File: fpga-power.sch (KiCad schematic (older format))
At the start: 43 parts, among them U1 XC7K70T-FBG484

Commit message: Change VCC labels
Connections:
- net labels added: VDD1, VDD2
- net labels removed: VCC1V1, VCC1V8
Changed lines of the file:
@@
 	1    0    0    -1
 $EndComp
-Text GLabel 7525 2275 1    50   Input ~ 0
-VCC1V8
 $Comp
 L lpddr4-test-board:XC7K70T-FBG484 U1
@@
 Wire Wire Line
 	7525 3425 7275 3425
-Text GLabel 7275 3425 0    50   Input ~ 0
-VCC1V8
 Connection ~ 7525 3625
 Wire Wire Line
@@
 	7525 3525 7525 3625
 Connection ~ 7525 3525
-Text GLabel 7275 3525 0    50   Input ~ 0
-VCC1V1
 Connection ~ 9525 2525
 Wire Wire Line
@@
 	1    0    0    -1
 $EndComp
-Text GLabel 5025 5525 1    50   Input ~ 10
+Text GLabel 5025 5525 1    50   Input ~ 0
 VCC3V3
-Text GLabel 5275 5525 1    50   Input ~ 10
-VCC3V3
-Text GLabel 5525 5525 1    50   Input ~ 10
-VCC3V3
-Text GLabel 5775 5525 1    50   Input ~ 10
-VCC3V3
-Text GLabel 6025 5525 1    50   Input ~ 10
-VCC3V3
-Text GLabel 6275 5525 1    50   Input ~ 10
-VDDQ
-Text GLabel 6525 5525 1    50   Input ~ 10
+Text GLabel 6275 5525 1    50   Input ~ 0
 VDDQ
 Wire Notes Line
@@
 Text Notes 9750 1925 3    50   ~ 0
 VCCINT max: 1.1V
-Text GLabel 9525 2225 1    50   Input ~ 0
-VCC1V1
-Text GLabel 14625 2250 1    50   Input ~ 0
-VCC1V1
 $Comp
 L lpddr4-test-board:XC7K70T-FBG484 U1
@@
 	1    0    0    -1
 $EndComp
-Text GLabel 4700 2225 1    50   Input ~ 0
-VCC1V8
 $Comp
 L lpddr4-test-board:GND #PWR0115
@@
 	1    0    0    -1
 $EndComp
-Text GLabel 4975 2225 1    50   Input ~ 0
-VCC1V8
 $Comp
 L lpddr4-test-board:GND #PWR0116
@@
 	1    0    0    -1
 $EndComp
-Text GLabel 5525 2225 1    50   Input ~ 0
-VCC1V8
 $Comp
 L lpddr4-test-board:GND #PWR0123
@@
 	1    0    0    -1
 $EndComp
-Text GLabel 5800 2225 1    50   Input ~ 0
-VCC1V8
 $Comp
 L lpddr4-test-board:GND #PWR0172
@@
 	1    0    0    -1
 $EndComp
-Text GLabel 6075 2225 1    50   Input ~ 0
-VCC1V8
 $Comp
 L lpddr4-test-board:GND #PWR0173
@@
 $EndComp
 Text GLabel 6350 2225 1    50   Input ~ 0
-VCC1V8
+VDD1
 $Comp
 L lpddr4-test-board:GND #PWR0193
@@
 Wire Wire Line
 	6350 2350 6350 2225
-Text GLabel 10175 2250 1    50   Input ~ 0
-VCC1V1
-Text GLabel 10450 2250 1    50   Input ~ 0
-VCC1V1
-Text GLabel 10725 2250 1    50   Input ~ 0
-VCC1V1
-Text GLabel 11000 2250 1    50   Input ~ 0
-VCC1V1
-Text GLabel 11275 2250 1    50   Input ~ 0
-VCC1V1
 $Comp
 L antmicroCapacitorsmisc:C_100n_0201 C62
@@
 Wire Wire Line
 	12650 2375 12650 2250
-Text GLabel 11550 2250 1    50   Input ~ 0
-VCC1V1
-Text GLabel 11825 2250 1    50   Input ~ 0
-VCC1V1
-Text GLabel 12100 2250 1    50   Input ~ 0
-VCC1V1
-Text GLabel 12375 2250 1    50   Input ~ 0
-VCC1V1
-Text GLabel 12650 2250 1    50   Input ~ 0
-VCC1V1
 $Comp
 L antmicroCapacitorsmisc:C_100n_0201 C67
@@
 Wire Wire Line
 	13725 2375 13725 2250
-Text GLabel 12900 2250 1    50   Input ~ 0
-VCC1V1
-Text GLabel 13175 2250 1    50   Input ~ 0
-VCC1V1
-Text GLabel 13450 2250 1    50   Input ~ 0
-VCC1V1
-Text GLabel 13725 2250 1    50   Input ~ 0
-VCC1V1
 Wire Wire Line
 	14625 2800 14625 2675
-Text GLabel 7275 3325 0    50   Input ~ 0
-VCC1V8
 $Comp
 L lpddr4-test-board:GND #PWR0204
@@
 	1    0    0    -1
 $EndComp
-Text GLabel 4700 3700 1    50   Input ~ 0
-VCC1V8
 $Comp
 L lpddr4-test-board:GND #PWR0205
@@
 	1    0    0    -1
 $EndComp
-Text GLabel 4975 3700 1    50   Input ~ 0
-VCC1V8
 $Comp
 L lpddr4-test-board:GND #PWR0206
@@
 Wire Wire Line
 	5825 3800 5825 3675
-Text GLabel 5275 3675 1    50   Input ~ 0
-VCC1V1
-Text GLabel 5550 3675 1    50   Input ~ 0
-VCC1V1
-Text GLabel 5825 3675 1    50   Input ~ 0
-VCC1V1
 Wire Wire Line
 	5275 3800 5275 3675
-Text GLabel 2675 2225 1    50   Input ~ 0
-VCC1V8
 Wire Wire Line
 	2675 2350 2675 2225
-Text GLabel 2950 2225 1    50   Input ~ 0
-VCC1V8
 Wire Wire Line
 	2950 2350 2950 2225
-Text GLabel 3225 2225 1    50   Input ~ 0
-VCC1V8
 Wire Wire Line
 	3225 2350 3225 2225
-Text GLabel 3500 2225 1    50   Input ~ 0
-VCC1V8
 Wire Wire Line
 	3500 2350 3500 2225
-Text GLabel 3775 2225 1    50   Input ~ 0
-VCC1V8
 Wire Wire Line
 	3775 2350 3775 2225
@@
 Wire Wire Line
 	3775 3775 3775 3650
+Wire Wire Line
+	3225 3775 3225 3650
+Text GLabel 6075 2225 1    50   Input ~ 0
+VDD1
+Text GLabel 5800 2225 1    50   Input ~ 0
+VDD1
+Text GLabel 5525 2225 1    50   Input ~ 0
+VDD1
+Text GLabel 5250 2225 1    50   Input ~ 0
+VDD1
+Text GLabel 4975 2225 1    50   Input ~ 0
+VDD1
+Text GLabel 4700 2225 1    50   Input ~ 0
+VDD1
+Text GLabel 3775 2225 1    50   Input ~ 0
+VDD1
+Text GLabel 3500 2225 1    50   Input ~ 0
+VDD1
+Text GLabel 3225 2225 1    50   Input ~ 0
+VDD1
+Text GLabel 2950 2225 1    50   Input ~ 0
+VDD1
+Text GLabel 2675 2225 1    50   Input ~ 0
+VDD1
+Text GLabel 4975 3700 1    50   Input ~ 0
+VDD1
+Text GLabel 4700 3700 1    50   Input ~ 0
+VDD1
+Text GLabel 7525 2275 1    50   Input ~ 0
+VDD1
+Text GLabel 7275 3425 0    50   Input ~ 0
+VDD1
+Text GLabel 7275 3325 0    50   Input ~ 0
+VDD1
+Text GLabel 10725 2250 1    50   Input ~ 0
+VDD2
+Text GLabel 10175 2250 1    50   Input ~ 0
+VDD2
+Text GLabel 10450 2250 1    50   Input ~ 0
+VDD2
+Text GLabel 11550 2250 1    50   Input ~ 0
+VDD2
+Text GLabel 11000 2250 1    50   Input ~ 0
+VDD2
+Text GLabel 11275 2250 1    50   Input ~ 0
+VDD2
+Text GLabel 12375 2250 1    50   Input ~ 0
+VDD2
+Text GLabel 11825 2250 1    50   Input ~ 0
+VDD2
+Text GLabel 12100 2250 1    50   Input ~ 0
+VDD2
+Text GLabel 13200 2250 1    50   Input ~ 0
+VDD2
+Text GLabel 12650 2250 1    50   Input ~ 0
+VDD2
+Text GLabel 12925 2250 1    50   Input ~ 0
+VDD2
 Text GLabel 3225 3650 1    50   Input ~ 0
-VCC1V1
+VDD2
+Text GLabel 13450 2250 1    50   Input ~ 0
+VDD2
+Text GLabel 13725 2250 1    50   Input ~ 0
+VDD2
+Text GLabel 14625 2250 1    50   Input ~ 0
+VDD2
 Text GLabel 3500 3650 1    50   Input ~ 0
-VCC1V1
+VDD2
 Text GLabel 3775 3650 1    50   Input ~ 0
-VCC1V1
-Wire Wire Line
-	3225 3775 3225 3650
-Text GLabel 5250 2225 1    50   Input ~ 0
-VCC1V8
+VDD2
+Text GLabel 7275 3525 0    50   Input ~ 0
+VDD2
+Text GLabel 5825 3675 1    50   Input ~ 0
+VDD2
+Text GLabel 5275 3675 1    50   Input ~ 0
+VDD2
+Text GLabel 5550 3675 1    50   Input ~ 0
+VDD2
+Text GLabel 9525 2225 1    50   Input ~ 0
+VDD2
+Text GLabel 5275 5525 1    50   Input ~ 0
+VCC3V3
+Text GLabel 5525 5525 1    50   Input ~ 0
+VCC3V3
+Text GLabel 5775 5525 1    50   Input ~ 0
+VCC3V3
+Text GLabel 6025 5525 1    50   Input ~ 0
+VCC3V3
+Text GLabel 6525 5525 1    50   Input ~ 0
+VDDQ
 $EndSCHEMATC

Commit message: Replace VCC3V3 with 3V3_SYS
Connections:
- net labels added: 3V3_SYS
- net labels removed: VCC3V3
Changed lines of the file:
@@
 $EndComp
 Text GLabel 5025 5525 1    50   Input ~ 0
-VCC3V3
+3V3_SYS
 Text GLabel 6275 5525 1    50   Input ~ 0
 VDDQ
@@
 VDD2
 Text GLabel 5275 5525 1    50   Input ~ 0
-VCC3V3
+3V3_SYS
 Text GLabel 5525 5525 1    50   Input ~ 0
-VCC3V3
+3V3_SYS
 Text GLabel 5775 5525 1    50   Input ~ 0
-VCC3V3
+3V3_SYS
 Text GLabel 6025 5525 1    50   Input ~ 0
-VCC3V3
+3V3_SYS
 Text GLabel 6525 5525 1    50   Input ~ 0
 VDDQ

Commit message: Introduce unified 1V1_SYS 1V8_SYS 3V3_SYS
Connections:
- net labels added: 1V1_SYS, 1V8_SYS
- net labels removed: VDD1, VDD2
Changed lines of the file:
@@
 $EndComp
 Text GLabel 6350 2225 1    50   Input ~ 0
-VDD1
+1V8_SYS
 $Comp
 L lpddr4-test-board:GND #PWR0193
@@
 	3225 3775 3225 3650
 Text GLabel 6075 2225 1    50   Input ~ 0
-VDD1
+1V8_SYS
 Text GLabel 5800 2225 1    50   Input ~ 0
-VDD1
+1V8_SYS
 Text GLabel 5525 2225 1    50   Input ~ 0
-VDD1
+1V8_SYS
 Text GLabel 5250 2225 1    50   Input ~ 0
-VDD1
+1V8_SYS
 Text GLabel 4975 2225 1    50   Input ~ 0
-VDD1
+1V8_SYS
 Text GLabel 4700 2225 1    50   Input ~ 0
-VDD1
+1V8_SYS
 Text GLabel 3775 2225 1    50   Input ~ 0
-VDD1
+1V8_SYS
 Text GLabel 3500 2225 1    50   Input ~ 0
-VDD1
+1V8_SYS
 Text GLabel 3225 2225 1    50   Input ~ 0
-VDD1
+1V8_SYS
 Text GLabel 2950 2225 1    50   Input ~ 0
-VDD1
+1V8_SYS
 Text GLabel 2675 2225 1    50   Input ~ 0
-VDD1
+1V8_SYS
 Text GLabel 4975 3700 1    50   Input ~ 0
-VDD1
+1V8_SYS
 Text GLabel 4700 3700 1    50   Input ~ 0
-VDD1
+1V8_SYS
 Text GLabel 7525 2275 1    50   Input ~ 0
-VDD1
+1V8_SYS
 Text GLabel 7275 3425 0    50   Input ~ 0
-VDD1
+1V8_SYS
 Text GLabel 7275 3325 0    50   Input ~ 0
-VDD1
+1V8_SYS
 Text GLabel 10725 2250 1    50   Input ~ 0
-VDD2
+1V1_SYS
 Text GLabel 10175 2250 1    50   Input ~ 0
-VDD2
+1V1_SYS
 Text GLabel 10450 2250 1    50   Input ~ 0
-VDD2
+1V1_SYS
 Text GLabel 11550 2250 1    50   Input ~ 0
-VDD2
+1V1_SYS
 Text GLabel 11000 2250 1    50   Input ~ 0
-VDD2
+1V1_SYS
 Text GLabel 11275 2250 1    50   Input ~ 0
-VDD2
+1V1_SYS
 Text GLabel 12375 2250 1    50   Input ~ 0
-VDD2
+1V1_SYS
 Text GLabel 11825 2250 1    50   Input ~ 0
-VDD2
+1V1_SYS
 Text GLabel 12100 2250 1    50   Input ~ 0
-VDD2
+1V1_SYS
 Text GLabel 13200 2250 1    50   Input ~ 0
-VDD2
+1V1_SYS
 Text GLabel 12650 2250 1    50   Input ~ 0
-VDD2
+1V1_SYS
 Text GLabel 12925 2250 1    50   Input ~ 0
-VDD2
+1V1_SYS
 Text GLabel 3225 3650 1    50   Input ~ 0
-VDD2
+1V1_SYS
 Text GLabel 13450 2250 1    50   Input ~ 0
-VDD2
+1V1_SYS
 Text GLabel 13725 2250 1    50   Input ~ 0
-VDD2
+1V1_SYS
 Text GLabel 14625 2250 1    50   Input ~ 0
-VDD2
+1V1_SYS
 Text GLabel 3500 3650 1    50   Input ~ 0
-VDD2
+1V1_SYS
 Text GLabel 3775 3650 1    50   Input ~ 0
-VDD2
+1V1_SYS
 Text GLabel 7275 3525 0    50   Input ~ 0
-VDD2
+1V1_SYS
 Text GLabel 5825 3675 1    50   Input ~ 0
-VDD2
+1V1_SYS
 Text GLabel 5275 3675 1    50   Input ~ 0
-VDD2
+1V1_SYS
 Text GLabel 5550 3675 1    50   Input ~ 0
-VDD2
+1V1_SYS
 Text GLabel 9525 2225 1    50   Input ~ 0
-VDD2
+1V1_SYS
 Text GLabel 5275 5525 1    50   Input ~ 0
 3V3_SYS

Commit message: Update component library
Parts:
- C11, C47, C48, C49, C50, C51, C52, C53, C54, C55, C56, C57, C58, C59, C60, C61, C62, C63, C64, C65, C66, C67, C68, C69, C70, C9: footprint antmicro-footprints:0201-res -> lpddr4-test-board-footprints:0201-res; symbol antmicroCapacitorsmisc:C_100n_0201 -> lpddr4-test-board:C_100n_0201

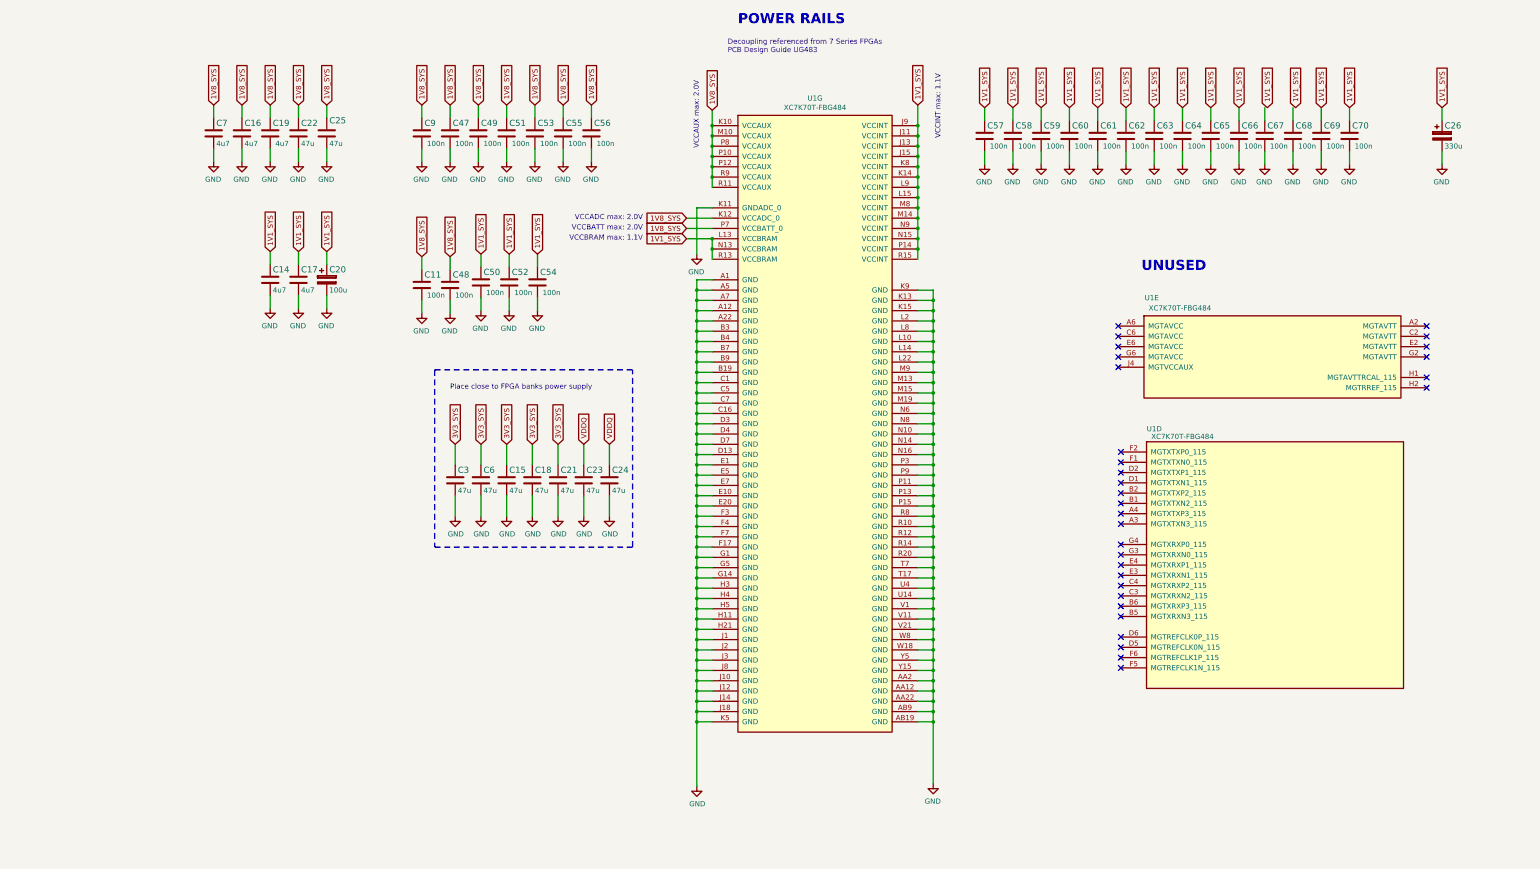
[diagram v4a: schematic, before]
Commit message: Add filtering capacitors, DRC clean
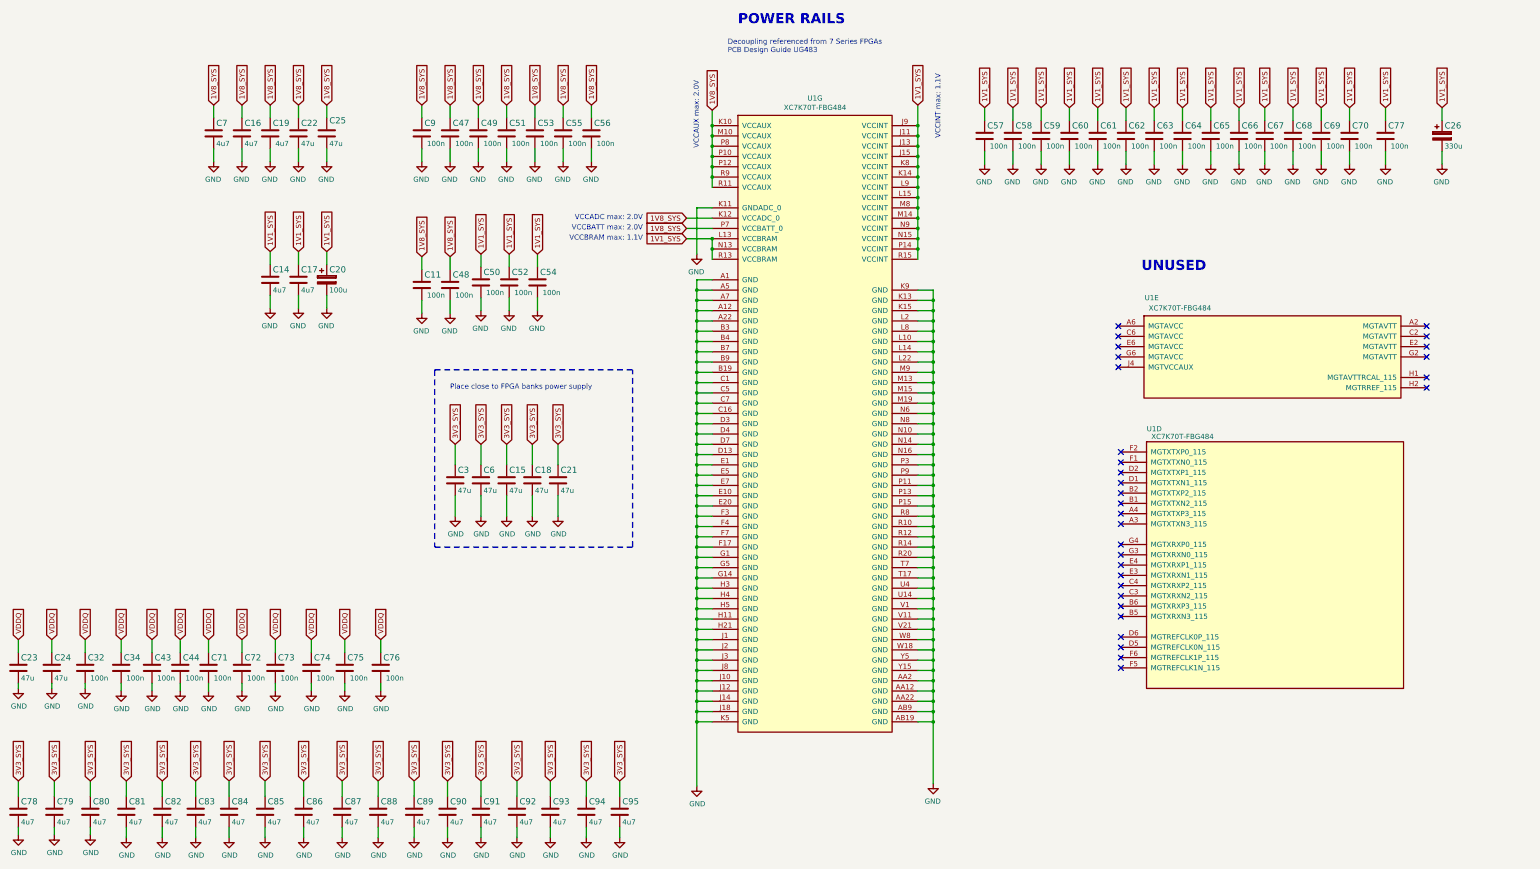
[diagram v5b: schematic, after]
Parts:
- added C32, C34, C43, C44, C71, C72, C73, C74, C75, C76, C77: C_100n_0201, lpddr4-test-board-footprints:0201-res, symbol lpddr4-test-board:C_100n_0201
- added C78, C79, C80, C81, C82, C83, C84, C85, C86, C87, C88, C89, C90, C91, C92, C93, C94, C95: C_4u7_0402, lpddr4-test-board-footprints:0402-cap, symbol lpddr4-test-board:C_4u7_0402
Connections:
- net 1V1_SYS: now also C67.1, C68.1, C77.1
- net 3V3_SYS: now also C78.1, C79.1, C80.1, C81.1, C82.1, C83.1, C84.1, C85.1, C86.1, C87.1, C88.1, C89.1, C90.1, C91.1, C92.1, C93.1, C94.1, C95.1
- net GND: now also C32.2, C34.2, C43.2, C44.2, C71.2, C72.2, C73.2, C74.2, C75.2, C76.2, C77.2, C78.2, C79.2, C80.2, C81.2, C82.2, C83.2, C84.2, C85.2, C86.2, C87.2, C88.2, C89.2, C90.2, C91.2, C92.2, C93.2, C94.2, C95.2
- net VDDQ: now also C32.1, C34.1, C43.1, C44.1, C71.1, C72.1, C73.1, C74.1, C75.1, C76.1
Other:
- moved on the sheet: C23, C24

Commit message: Connect VCCINT into 1V0_SYS, split power plane
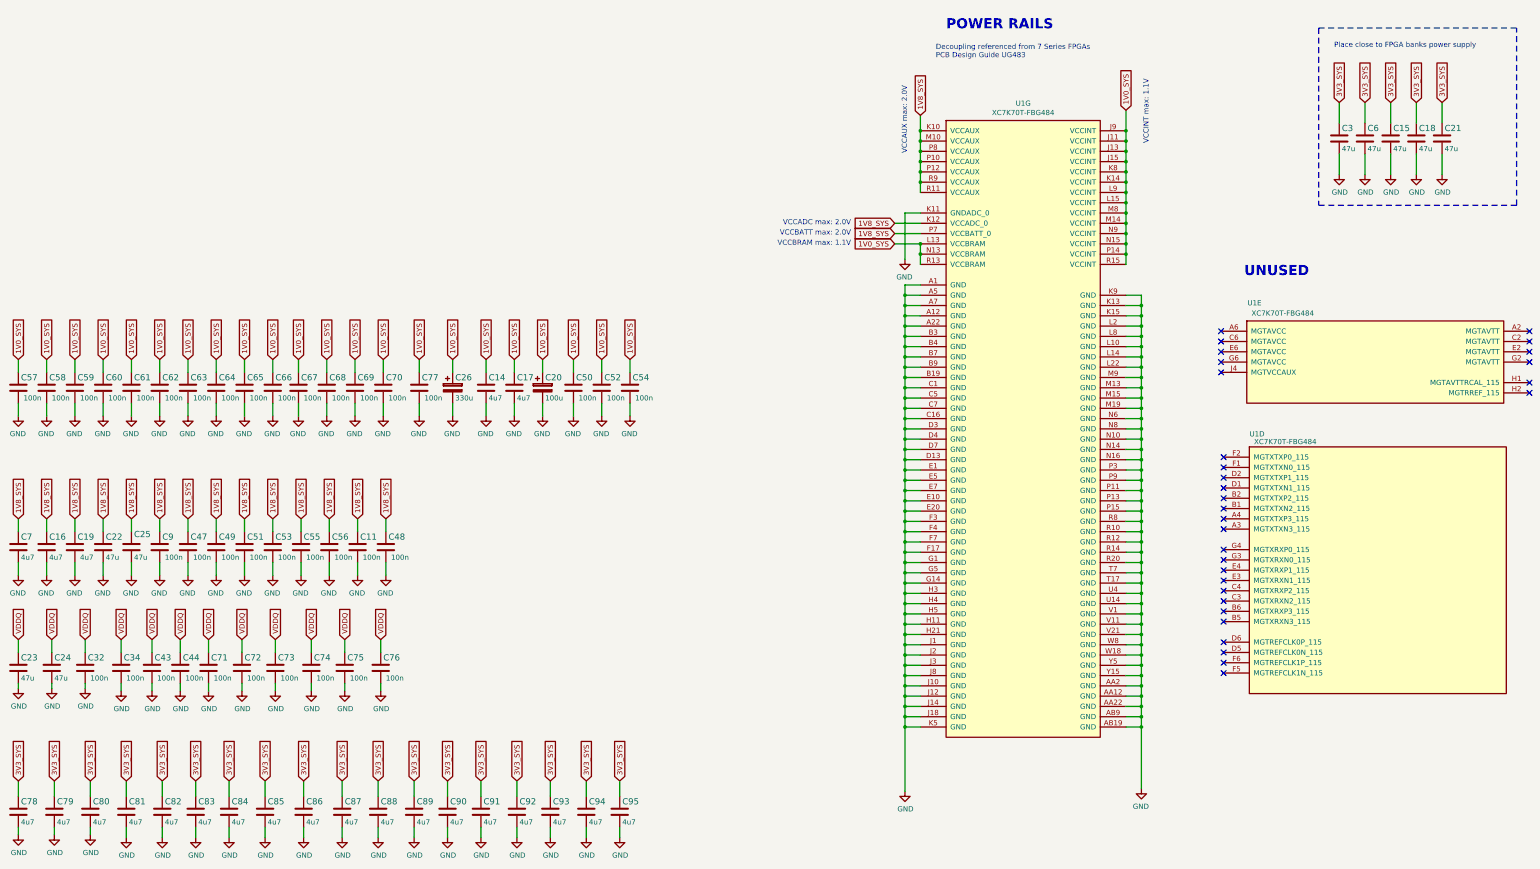
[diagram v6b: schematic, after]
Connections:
- net 1V1_SYS renamed 1V0_SYS
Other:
- moved on the sheet: C11, C14, C15, C16, C17, C18, C19, C20, C21, C22, C25, C26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
